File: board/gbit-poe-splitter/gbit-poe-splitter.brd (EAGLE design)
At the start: 61.3 x 42.2 mm, 51 parts, among them IC1 LM2596HVS, U1 TPS2379DDA

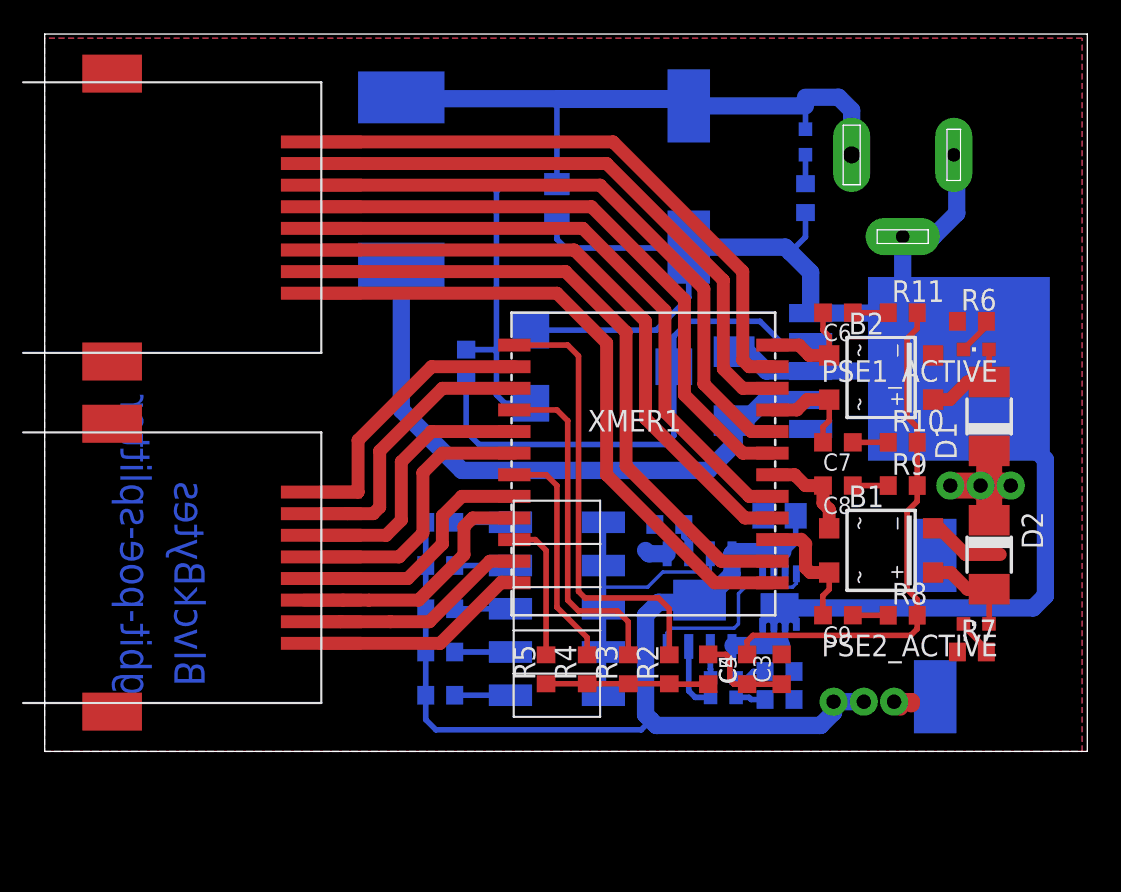
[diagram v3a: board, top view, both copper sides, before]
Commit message: Fixed jack orientation, font and keepouts
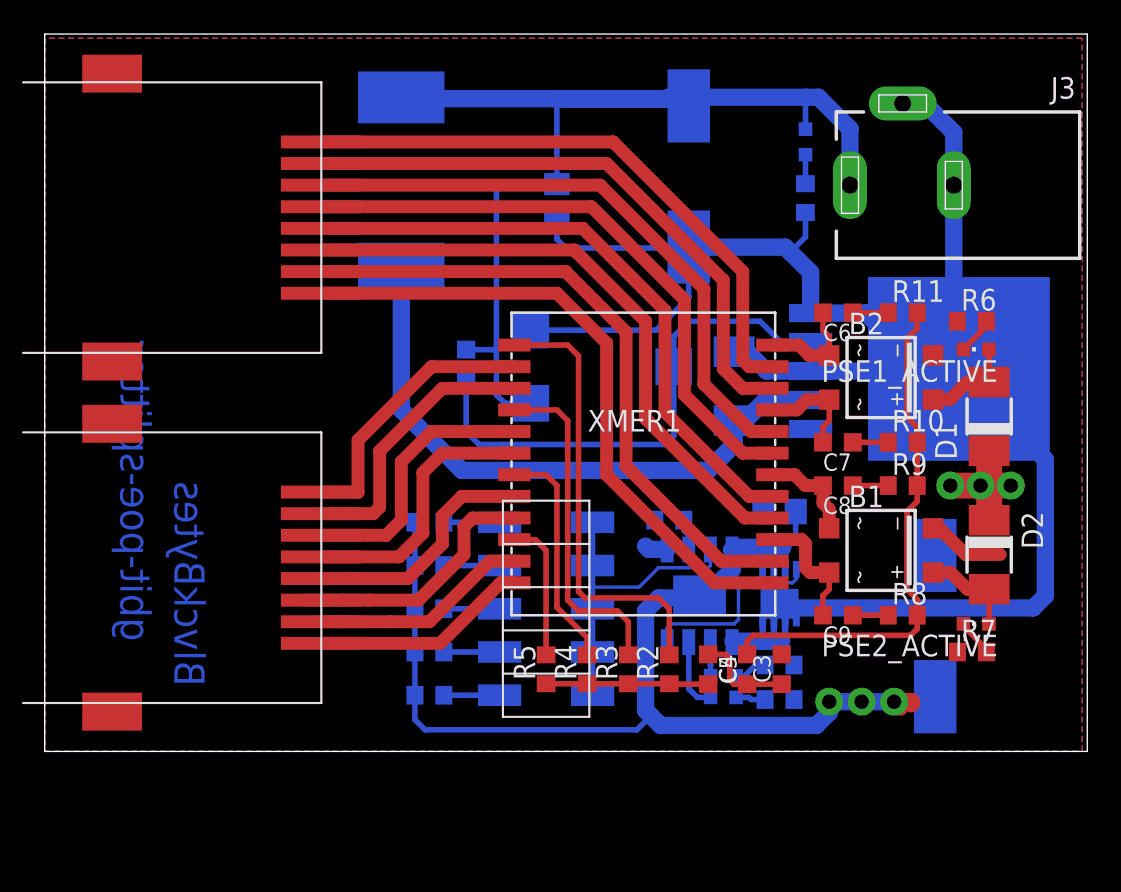
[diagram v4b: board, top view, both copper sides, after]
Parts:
- removed J1: (no value), con-jack:SPC4078
- added J3: (no value), con-jack:DCJ0303
- moved CLASS-SEL 0.64 mm to (29.5, 14.7)
- moved R1 0.63 mm to (22.6, 9.65)
- moved R15 0.63 mm to (22.6, 12.2)
- moved R16 0.63 mm to (22.6, 14.7)
- moved R17 0.63 mm to (22.6, 17.3)
- moved R18 0.63 mm to (22.6, 19.8)
- moved R13 0.38 mm to (43.2, 11.4)
- moved R19 0.25 mm to (36.7, 19.9)
- moved U$1 0.25 mm to (43.2, 15.6)
- moved U1 0.25 mm to (38.5, 15.5)
- moved C10 0.25 mm to (43.2, 20.4)
- moved INRUSH_LIMITED 0.13 mm to (39.9, 10.8)
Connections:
- net POWER: now also J3.1; no longer J1.3
- net RTN: now also J3.2, J3.3; no longer J1.1, J1.2
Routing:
- net RTN: track 117.0 -> 128.1 mm
- net GND: track 70.9 -> 73.5 mm
- net POWER: track 64.1 -> 66.4 mm
- net R_CLS: track 17.8 -> 18.6 mm

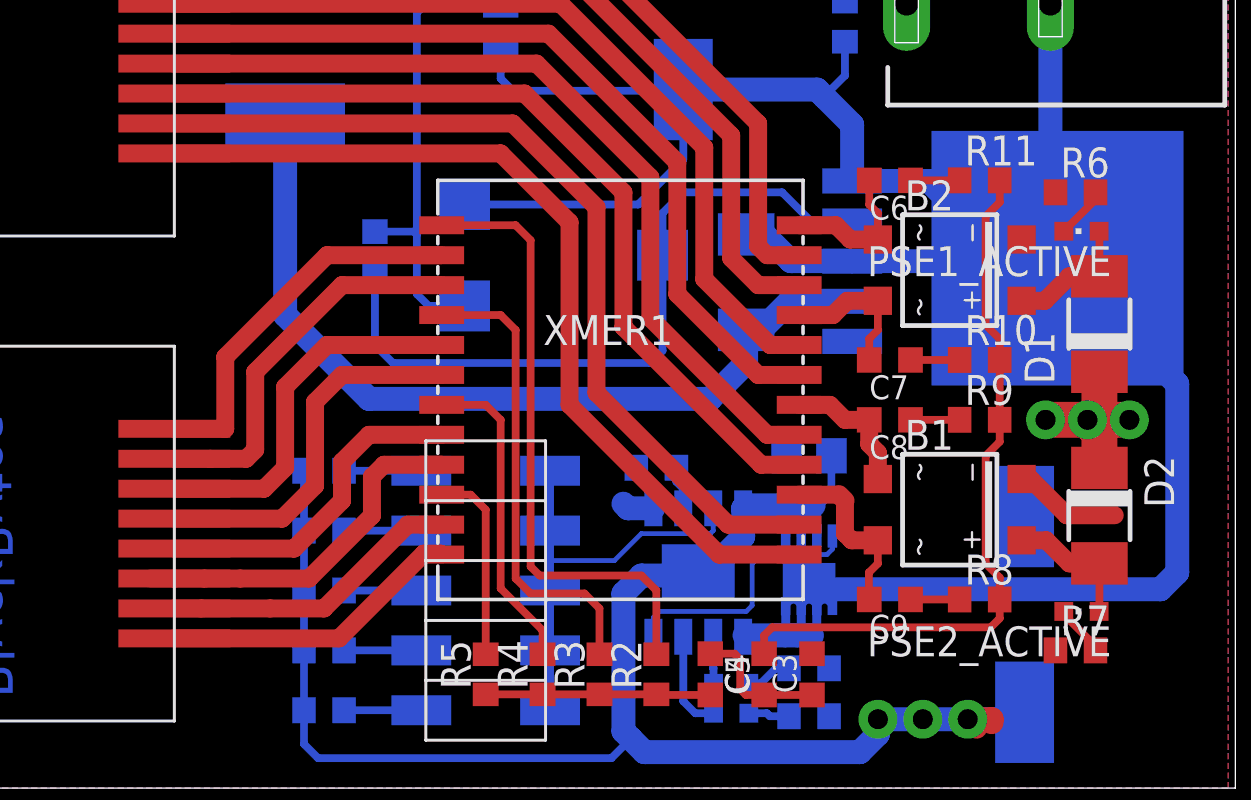
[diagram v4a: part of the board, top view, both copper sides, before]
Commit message: Documented first physical prototype
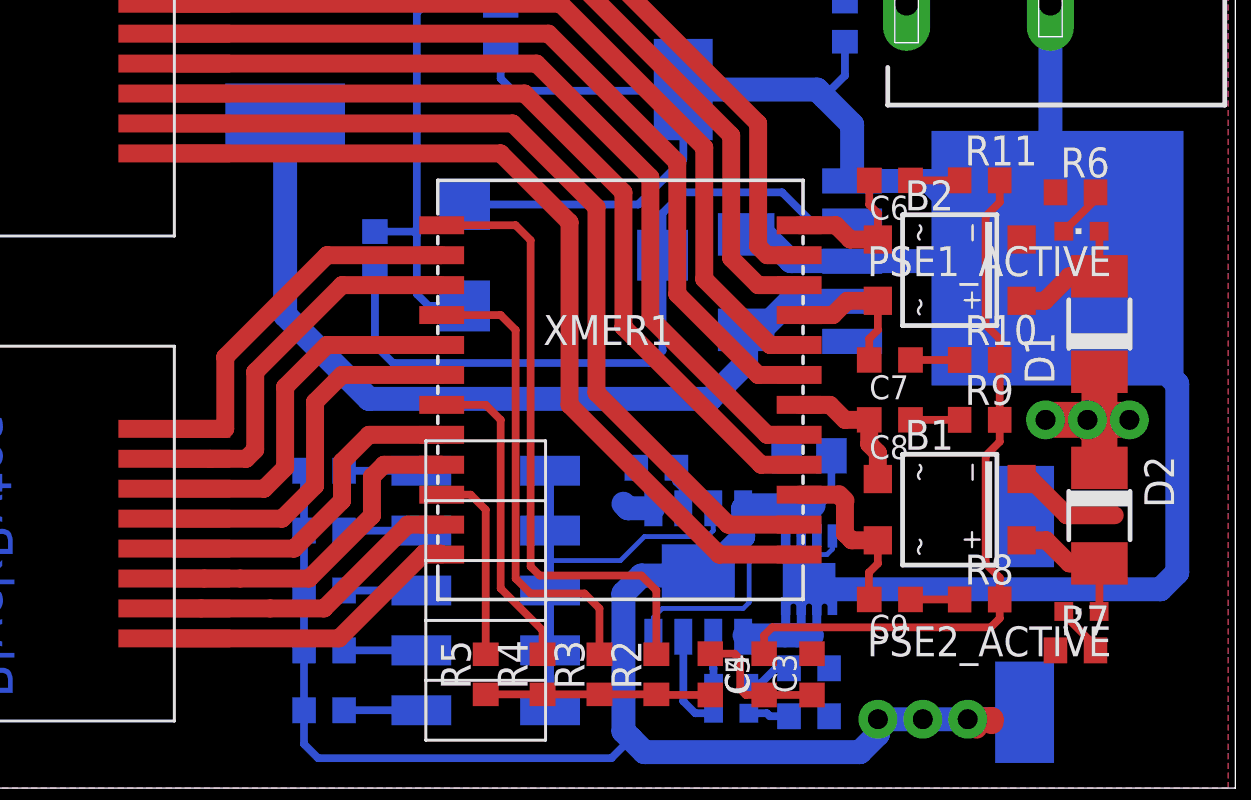
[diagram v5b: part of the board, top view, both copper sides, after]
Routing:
- net RTN: track 128.1 -> 125.4 mm
- net N$6: track 15.3 -> 14.3 mm
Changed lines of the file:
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@@
 <grid distance="50" unitdist="mil" unit="mil" style="lines" multiple="1" display="no" altdistance="5" altunitdist="mil" altunit="mil"/>
 <layers>
-<layer number="1" name="Top" color="4" fill="1" visible="yes" active="yes"/>
+<layer number="1" name="Top" color="4" fill="1" visible="no" active="yes"/>
 <layer number="16" name="Bottom" color="1" fill="1" visible="yes" active="yes"/>
 <layer number="17" name="Pads" color="2" fill="1" visible="yes" active="yes"/>
 <layer number="18" name="Vias" color="2" fill="1" visible="yes" active="yes"/>
 <layer number="19" name="Unrouted" color="6" fill="1" visible="yes" active="yes"/>
-<layer number="20" name="Dimension" color="24" fill="1" visible="yes" active="yes"/>
-<layer number="21" name="tPlace" color="7" fill="1" visible="yes" active="yes"/>
-<layer number="22" name="bPlace" color="7" fill="1" visible="yes" active="yes"/>
-<layer number="23" name="tOrigins" color="15" fill="1" visible="yes" active="yes"/>
-<layer number="24" name="bOrigins" color="15" fill="1" visible="yes" active="yes"/>
-<layer number="25" name="tNames" color="7" fill="1" visible="yes" active="yes"/>
-<layer number="26" name="bNames" color="7" fill="1" visible="yes" active="yes"/>
+<layer number="20" name="Dimension" color="24" fill="1" visible="no" active="yes"/>
+<layer number="21" name="tPlace" color="7" fill="1" visible="no" active="yes"/>
+<layer number="22" name="bPlace" color="7" fill="1" visible="no" active="yes"/>
+<layer number="23" name="tOrigins" color="15" fill="1" visible="no" active="yes"/>
+<layer number="24" name="bOrigins" color="15" fill="1" visible="no" active="yes"/>
+<layer number="25" name="tNames" color="7" fill="1" visible="no" active="yes"/>
+<layer number="26" name="bNames" color="7" fill="1" visible="no" active="yes"/>
 <layer number="27" name="tValues" color="7" fill="1" visible="no" active="yes"/>
 <layer number="28" name="bValues" color="7" fill="1" visible="no" active="yes"/>
@@
 <layer number="37" name="tTest" color="7" fill="1" visible="no" active="yes"/>
 <layer number="38" name="bTest" color="7" fill="1" visible="no" active="yes"/>
-<layer number="39" name="tKeepout" color="4" fill="11" visible="yes" active="yes"/>
-<layer number="40" name="bKeepout" color="1" fill="11" visible="yes" active="yes"/>
-<layer number="41" name="tRestrict" color="4" fill="10" visible="yes" active="yes"/>
-<layer number="42" name="bRestrict" color="1" fill="10" visible="yes" active="yes"/>
+<layer number="39" name="tKeepout" color="4" fill="11" visible="no" active="yes"/>
+<layer number="40" name="bKeepout" color="1" fill="11" visible="no" active="yes"/>
+<layer number="41" name="tRestrict" color="4" fill="10" visible="no" active="yes"/>
+<layer number="42" name="bRestrict" color="1" fill="10" visible="no" active="yes"/>
 <layer number="43" name="vRestrict" color="2" fill="10" visible="no" active="yes"/>
 <layer number="44" name="Drills" color="7" fill="1" visible="no" active="yes"/>
@@
 <layer number="49" name="Reference" color="7" fill="1" visible="no" active="yes"/>
 <layer number="50" name="dxf" color="7" fill="1" visible="no" active="no"/>
-<layer number="51" name="tDocu" color="7" fill="1" visible="yes" active="yes"/>
-<layer number="52" name="bDocu" color="7" fill="1" visible="yes" active="yes"/>
+<layer number="51" name="tDocu" color="7" fill="1" visible="no" active="yes"/>
+<layer number="52" name="bDocu" color="7" fill="1" visible="no" active="yes"/>
 <layer number="53" name="tGND_GNDA" color="7" fill="9" visible="no" active="no"/>
 <layer number="54" name="bGND_GNDA" color="1" fill="9" visible="no" active="no"/>
@@
 </class>
 </classes>
-<designrules name="default">
+<designrules name="default *">
 <description language="de">&lt;b&gt;EAGLE Design Rules&lt;/b&gt;
 &lt;p&gt;
@@
 <param name="srMinRoundness" value="0mil"/>
 <param name="srMaxRoundness" value="0mil"/>
-<param name="slThermalIsolate" value="10mil"/>
+<param name="slThermalIsolate" value="20mil"/>
 <param name="slThermalsForVias" value="0"/>
 <param name="dpMaxLengthDifference" value="10mm"/>
@@
 <wire x1="19.05" y1="15.24" x2="21.971" y2="15.24" width="0.762" layer="1"/>
 <wire x1="25.146" y1="20.066" x2="24.638" y2="19.558" width="0.762" layer="1"/>
-<wire x1="15.24" y1="15.24" x2="16.256" y2="15.24" width="0.762" layer="1"/>
 <wire x1="17.526" y1="15.24" x2="16.256" y2="15.24" width="0.762" layer="1"/>
 </signal>
@@
 <contactref element="C8" pad="2"/>
 <contactref element="B1" pad="~1"/>
-<wire x1="45.72" y1="21.957" x2="45.734" y2="21.971" width="0.3302" layer="1"/>
 <wire x1="42.7609" y1="22.606" x2="44.069" y2="22.606" width="0.762" layer="1"/>
 <wire x1="44.704" y1="21.971" x2="45.734" y2="21.971" width="0.762" layer="1"/>
@@
 <contactref element="XMER1" pad="10"/>
 <contactref element="R5" pad="2"/>
-<wire x1="29.337" y1="12.153" x2="29.464" y2="12.026" width="0.3302" layer="1"/>
 <wire x1="29.464" y1="12.026" x2="29.464" y2="18.161" width="0.3302" layer="1"/>
 <wire x1="28.829" y1="18.796" x2="27.5971" y2="18.796" width="0.3302" layer="1"/>
@@
 <wire x1="54.222" y1="28.06" x2="55.499" y2="28.06" width="0.762" layer="1"/>
 <wire x1="53.183" y1="27.021" x2="54.222" y2="28.06" width="0.762" layer="1"/>
-<wire x1="55.748" y1="28.309" x2="55.499" y2="28.06" width="0.3302" layer="1"/>
 <wire x1="55.499" y1="28.06" x2="55.499" y2="29.96" width="0.3302" layer="1"/>
 <wire x1="55.499" y1="29.96" x2="55.487" y2="29.972" width="0.3302" layer="1"/>
@@
 <wire x1="32.1945" y1="9.652" x2="32.1945" y2="12.192" width="0.3302" layer="16"/>
 <wire x1="39.116" y1="18.21815" x2="39.116" y2="17.272" width="0.2032" layer="16"/>
-<wire x1="39.116" y1="17.272" x2="38.989" y2="17.145" width="0.2032" layer="16"/>
-<wire x1="36.068" y1="17.145" x2="34.925" y2="16.002" width="0.2032" layer="16"/>
-<wire x1="34.925" y1="16.002" x2="32.1945" y2="16.002" width="0.2032" layer="16"/>
-<wire x1="38.989" y1="17.145" x2="36.068" y2="17.145" width="0.2032" layer="16"/>
+<wire x1="39.116" y1="17.272" x2="38.862" y2="17.018" width="0.2032" layer="16"/>
+<wire x1="36.195" y1="17.018" x2="35.179" y2="16.002" width="0.2032" layer="16"/>
+<wire x1="35.179" y1="16.002" x2="32.1945" y2="16.002" width="0.2032" layer="16"/>
+<wire x1="38.862" y1="17.018" x2="36.195" y2="17.018" width="0.2032" layer="16"/>
 </signal>
 <signal name="N$29">
@@
 <wire x1="49.53" y1="32.1056" x2="48.26" y2="32.1056" width="1.016" layer="16"/>
 <wire x1="48.26" y1="32.1056" x2="45.0088" y2="32.1056" width="1.016" layer="16"/>
-<wire x1="50.673" y1="33.274" x2="50.419" y2="33.02" width="1.016" layer="16"/>
 <wire x1="50.419" y1="33.02" x2="50.0126" y2="32.6136" width="1.016" layer="16"/>
 <wire x1="49.403" y1="28.702" x2="45.0088" y2="28.702" width="1.016" layer="16"/>
@@
 <wire x1="49.53" y1="29.21" x2="49.53" y2="32.1056" width="1.016" layer="16"/>
 <wire x1="49.53" y1="32.1056" x2="49.53" y2="32.6136" width="1.016" layer="16"/>
-<wire x1="50.419" y1="30.988" x2="50.419" y2="33.02" width="1.016" layer="16"/>
 <wire x1="45.0088" y1="28.702" x2="42.411" y2="28.702" width="1.016" layer="16"/>
 <wire x1="42.411" y1="28.702" x2="41.275" y2="29.838" width="1.016" layer="16"/>
@@
 <wire x1="42.1894" y1="14.0716" x2="42.4688" y2="14.351" width="0.254" layer="16"/>
 <wire x1="42.4688" y1="14.351" x2="42.5704" y2="14.351" width="0.254" layer="16"/>
-<wire x1="42.5704" y1="14.351" x2="42.799" y2="14.351" width="0.254" layer="16"/>
 <wire x1="42.8498" y1="14.0716" x2="42.5704" y2="14.351" width="0.254" layer="16"/>
 <wire x1="42.8498" y1="14.0716" x2="43.18" y2="14.4018" width="0.254" layer="16"/>
@@
 <contactref element="U$1" pad="G"/>
 <wire x1="36.576" y1="12.76985" x2="36.576" y2="13.589" width="0.2032" layer="16"/>
-<wire x1="36.576" y1="13.589" x2="36.83" y2="13.843" width="0.2032" layer="16"/>
-<wire x1="40.767" y1="15.875" x2="41.148" y2="16.256" width="0.2032" layer="16"/>
-<wire x1="41.148" y1="16.256" x2="43.942" y2="16.256" width="0.2032" layer="16"/>
+<wire x1="36.576" y1="13.589" x2="36.957" y2="13.97" width="0.2032" layer="16"/>
+<wire x1="40.64" y1="16.002" x2="40.894" y2="16.256" width="0.2032" layer="16"/>
+<wire x1="40.894" y1="16.256" x2="43.942" y2="16.256" width="0.2032" layer="16"/>
 <wire x1="43.942" y1="16.256" x2="44.1706" y2="16.4846" width="0.2032" layer="16"/>
 <wire x1="44.1706" y1="16.4846" x2="44.1706" y2="17.0434" width="0.2032" layer="16"/>
-<wire x1="36.83" y1="13.843" x2="40.513" y2="13.843" width="0.2032" layer="16"/>
-<wire x1="40.513" y1="13.843" x2="40.767" y2="14.097" width="0.2032" layer="16"/>
-<wire x1="40.767" y1="14.097" x2="40.767" y2="15.875" width="0.2032" layer="16"/>
+<wire x1="36.957" y1="13.97" x2="40.386" y2="13.97" width="0.2032" layer="16"/>
+<wire x1="40.386" y1="13.97" x2="40.64" y2="14.224" width="0.2032" layer="16"/>
+<wire x1="40.64" y1="14.224" x2="40.64" y2="16.002" width="0.2032" layer="16"/>
 </signal>
 <signal name="N$34">
